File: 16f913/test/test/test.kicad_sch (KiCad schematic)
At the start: 21 parts, among them IC1 PIC16873P P16f913, J1 MTA06-156, Q1 20.0MHz, T1 BC337, U1 CC56-12EWA

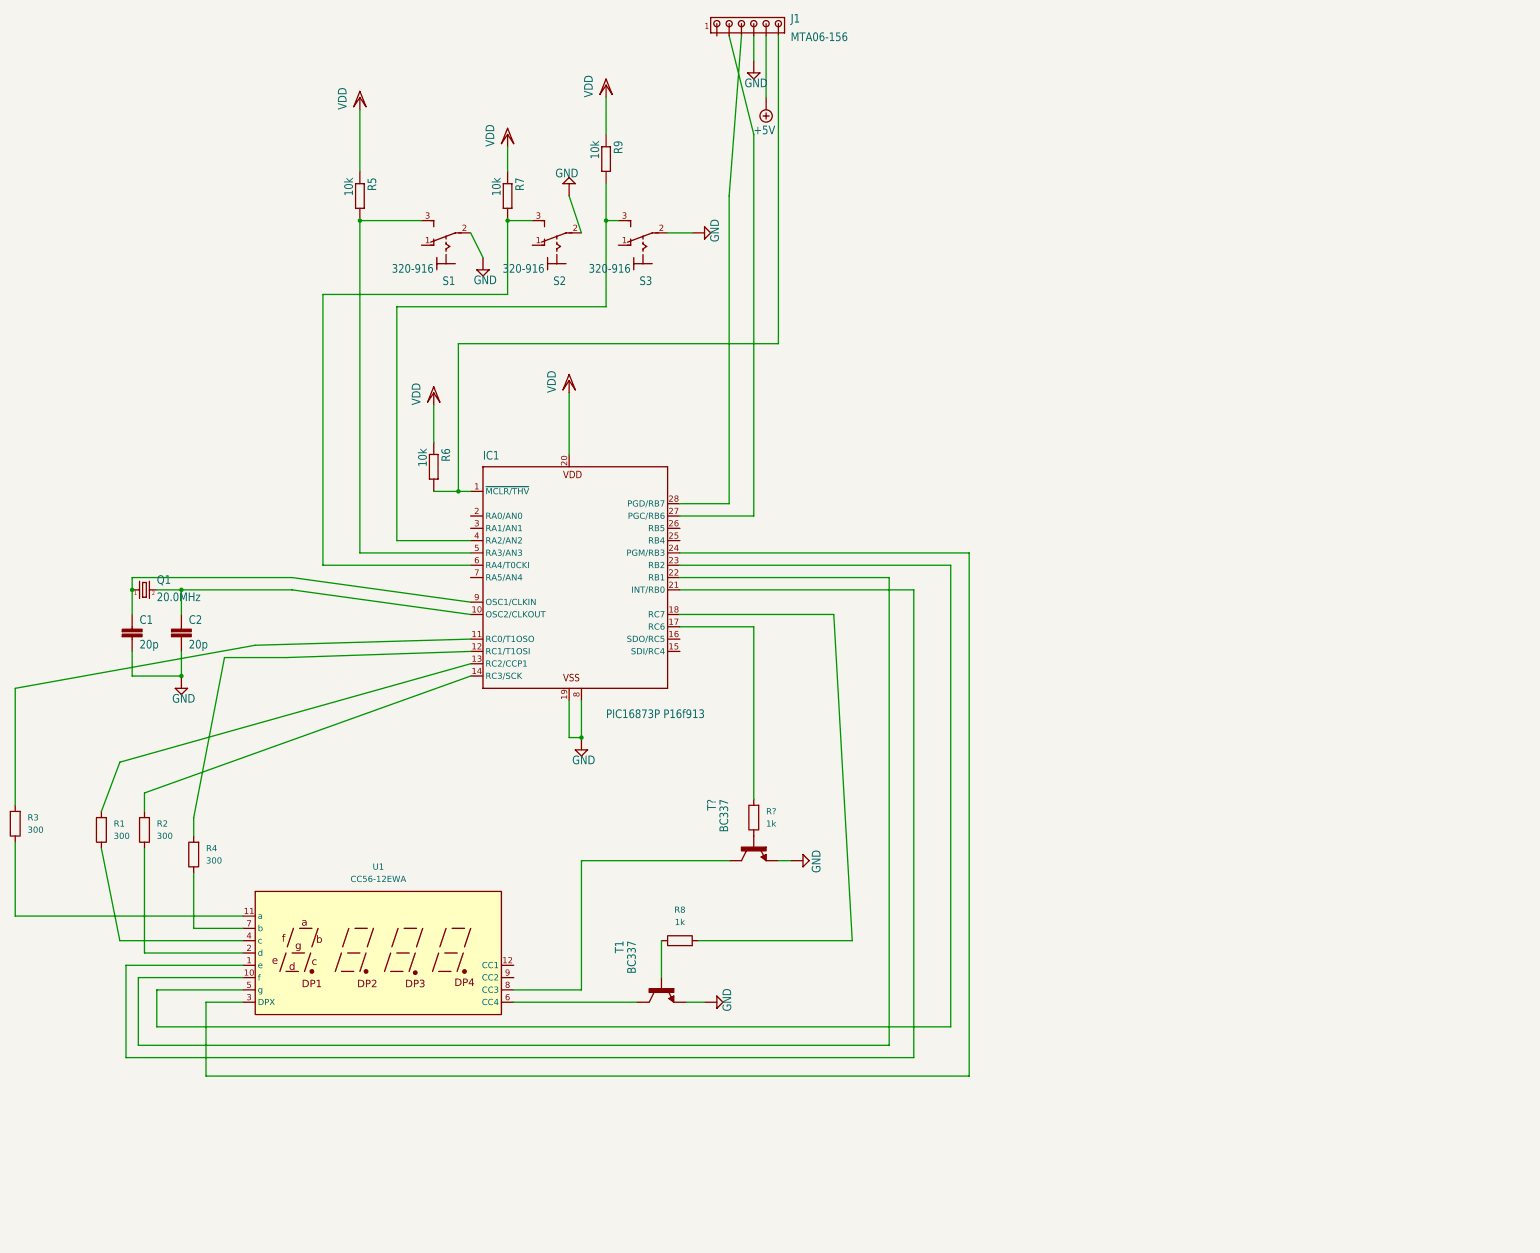
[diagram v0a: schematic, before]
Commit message: added wdg tests added more memory operations macros
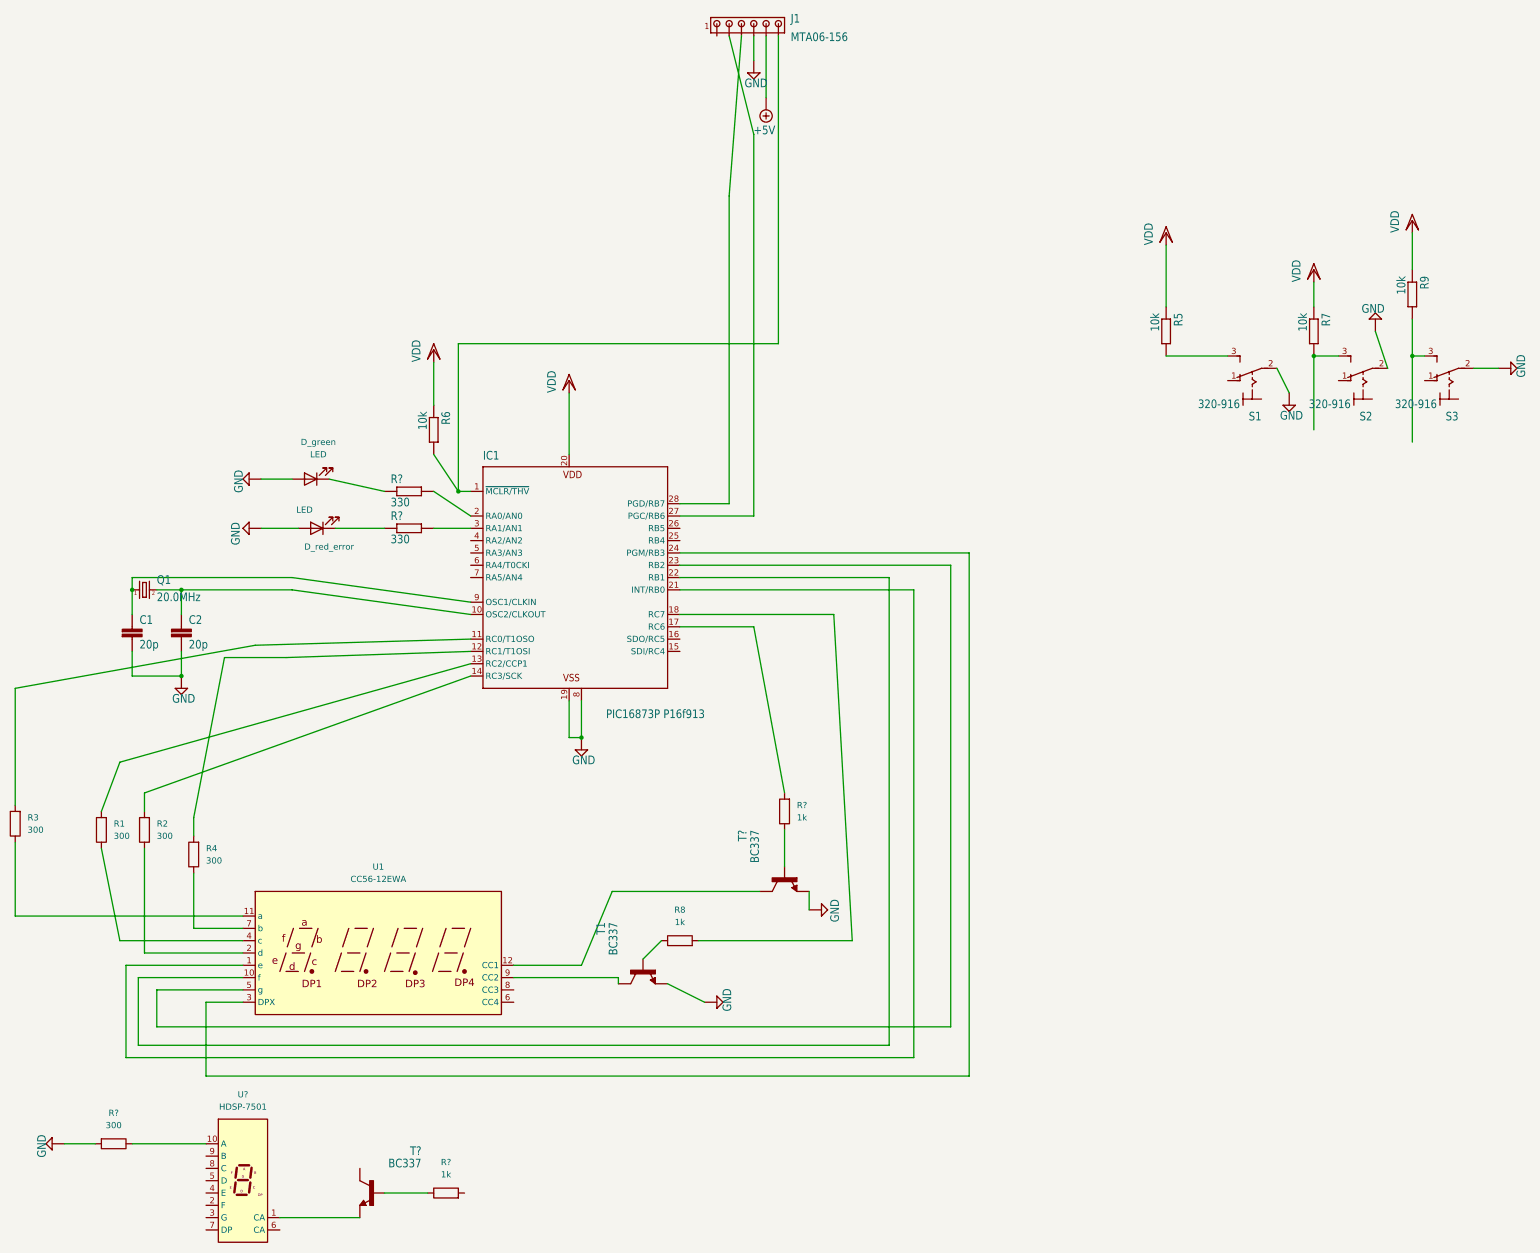
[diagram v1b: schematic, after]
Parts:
- added D_green, D_red_error: LED, symbol Device:LED
- added R?: 1k, symbol Device:R
- added R? (x2): 330, schemat_regulatora:0204_7, symbol schemat_regulatora-eagle-import:R-EU_0204/7
- added R?: 300, symbol Device:R
- added T?: BC337, schemat_regulatora:TO92, symbol schemat_regulatora-eagle-import:BC337
- added U?: HDSP-7501, Display_7Segment:HDSP-A151, symbol Display_Character:HDSP-7501
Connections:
- net GND: now also D_green.2 (A), D_red_error.2 (A), R?.2
- net at R9.2, S3.3 (S): no longer IC1.4 (RA2/AN2)
- net at T?.3 (C): now also U1.12 (CC1); no longer U1.8 (CC3)
- net at R7.2, S2.3 (S): no longer IC1.6 (RA4/T0CKI)
- net at R5.2, S1.3 (S): no longer IC1.5 (RA3/AN3)
- net at U1.6 (CC4): no longer T1.3 (C)
- net at U1.9 (CC2): now also T1.3 (C)
- net at IC1.2 (RA0/AN0): now also R?.2
- net at IC1.3 (RA1/AN1): now also R?.2
- new net: T?.1 (E), U?.1 (CA)
- new net: R?.1, U?.10 (A)
- new net: D_red_error.1 (K), R?.1
- new net: R?.1, T?.2 (B)
- new net: D_green.1 (K), R?.1
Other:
- moved on the sheet: R5, R6, R7, R9, R?, S1, S2, S3, T1, T?
